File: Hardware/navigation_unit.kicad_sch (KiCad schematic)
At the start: 34 parts, among them SW1 SW_SPDT, SW2 SW_Push_Dual, U4 STM32F405RGTx, Y1 25MHz

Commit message: hardware: reorganizing components, im fucked
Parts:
- C12, C13, C25: footprint Capacitor_SMD:C_0603_1608Metric -> Capacitor_SMD:C_0402_1005Metric
- C14: footprint Capacitor_SMD:C_1206_3216Metric_Pad1.33x1.80mm_HandSolder -> Capacitor_SMD:C_0603_1608Metric
- D4, D5, D6, D7: footprint LED_SMD:LED_0805_2012Metric_Pad1.15x1.40mm_HandSolder -> LED_SMD:LED_0402_1005Metric
- FB1: footprint Inductor_SMD:L_0805_2012Metric_Pad1.05x1.20mm_HandSolder -> Inductor_SMD:L_0402_1005Metric
- R10, R11, R12, R13, R14, R15, R16, R17, R18, R9: footprint Resistor_SMD:R_0603_1608Metric_Pad0.98x0.95mm_HandSolder -> Resistor_SMD:R_0402_1005Metric
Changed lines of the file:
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@@
 			)
 		)
-		(property "Footprint" "Resistor_SMD:R_0603_1608Metric_Pad0.98x0.95mm_HandSolder"
+		(property "Footprint" "Resistor_SMD:R_0402_1005Metric"
 			(at 228.092 139.7 90)
 			(effects
@@
 			)
 		)
-		(property "Footprint" "LED_SMD:LED_0805_2012Metric_Pad1.15x1.40mm_HandSolder"
+		(property "Footprint" "LED_SMD:LED_0402_1005Metric"
 			(at 166.37 138.43 0)
 			(effects
@@
 			)
 		)
-		(property "Footprint" "Capacitor_SMD:C_1206_3216Metric_Pad1.33x1.80mm_HandSolder"
+		(property "Footprint" "Capacitor_SMD:C_0603_1608Metric"
 			(at 141.9352 36.83 0)
 			(effects
@@
 			)
 		)
-		(property "Footprint" "Resistor_SMD:R_0603_1608Metric_Pad0.98x0.95mm_HandSolder"
+		(property "Footprint" "Resistor_SMD:R_0402_1005Metric"
 			(at 235.712 139.7 90)
 			(effects
@@
 			)
 		)
-		(property "Footprint" "Capacitor_SMD:C_0603_1608Metric"
+		(property "Footprint" "Capacitor_SMD:C_0402_1005Metric"
 			(at 40.3352 144.78 0)
 			(effects
@@
 			)
 		)
-		(property "Footprint" "LED_SMD:LED_0805_2012Metric_Pad1.15x1.40mm_HandSolder"
+		(property "Footprint" "LED_SMD:LED_0402_1005Metric"
 			(at 184.15 138.43 0)
 			(effects
@@
 			)
 		)
-		(property "Footprint" "Resistor_SMD:R_0603_1608Metric_Pad0.98x0.95mm_HandSolder"
+		(property "Footprint" "Resistor_SMD:R_0402_1005Metric"
 			(at 250.952 139.7 90)
 			(effects
@@
 			)
 		)
-		(property "Footprint" "Resistor_SMD:R_0603_1608Metric_Pad0.98x0.95mm_HandSolder"
+		(property "Footprint" "Resistor_SMD:R_0402_1005Metric"
 			(at 173.99 67.818 90)
 			(effects
@@
 			)
 		)
-		(property "Footprint" "Resistor_SMD:R_0603_1608Metric_Pad0.98x0.95mm_HandSolder"
+		(property "Footprint" "Resistor_SMD:R_0402_1005Metric"
 			(at 243.332 139.7 90)
 			(effects
@@
 			)
 		)
-		(property "Footprint" "Resistor_SMD:R_0603_1608Metric_Pad0.98x0.95mm_HandSolder"
+		(property "Footprint" "Resistor_SMD:R_0402_1005Metric"
 			(at 164.592 146.05 90)
 			(effects
@@
 			)
 		)
-		(property "Footprint" "LED_SMD:LED_0805_2012Metric_Pad1.15x1.40mm_HandSolder"
+		(property "Footprint" "LED_SMD:LED_0402_1005Metric"
 			(at 175.26 138.43 0)
 			(effects
@@
 			)
 		)
-		(property "Footprint" "Capacitor_SMD:C_0603_1608Metric"
+		(property "Footprint" "Capacitor_SMD:C_0402_1005Metric"
 			(at 30.1752 144.78 0)
 			(effects
@@
 			)
 		)
-		(property "Footprint" "Inductor_SMD:L_0805_2012Metric_Pad1.05x1.20mm_HandSolder"
+		(property "Footprint" "Inductor_SMD:L_0402_1005Metric"
 			(at 232.41 56.388 90)
 			(effects
@@
 			)
 		)
-		(property "Footprint" "Capacitor_SMD:C_0603_1608Metric"
+		(property "Footprint" "Capacitor_SMD:C_0402_1005Metric"
 			(at 249.8852 101.6 0)
 			(effects
@@
 			)
 		)
-		(property "Footprint" "Resistor_SMD:R_0603_1608Metric_Pad0.98x0.95mm_HandSolder"
+		(property "Footprint" "Resistor_SMD:R_0402_1005Metric"
 			(at 182.372 146.05 90)
 			(effects
@@
 			)
 		)
-		(property "Footprint" "LED_SMD:LED_0805_2012Metric_Pad1.15x1.40mm_HandSolder"
+		(property "Footprint" "LED_SMD:LED_0402_1005Metric"
 			(at 193.04 138.43 0)
 			(effects
@@
 			)
 		)
-		(property "Footprint" "Resistor_SMD:R_0603_1608Metric_Pad0.98x0.95mm_HandSolder"
+		(property "Footprint" "Resistor_SMD:R_0402_1005Metric"
 			(at 173.482 146.05 90)
 			(effects
@@
 			)
 		)
-		(property "Footprint" "Resistor_SMD:R_0603_1608Metric_Pad0.98x0.95mm_HandSolder"
+		(property "Footprint" "Resistor_SMD:R_0402_1005Metric"
 			(at 191.262 146.05 90)
 			(effects
@@
 			)
 		)
-		(property "Footprint" "Resistor_SMD:R_0603_1608Metric_Pad0.98x0.95mm_HandSolder"
+		(property "Footprint" "Resistor_SMD:R_0402_1005Metric"
 			(at 175.26 107.188 90)
 			(effects

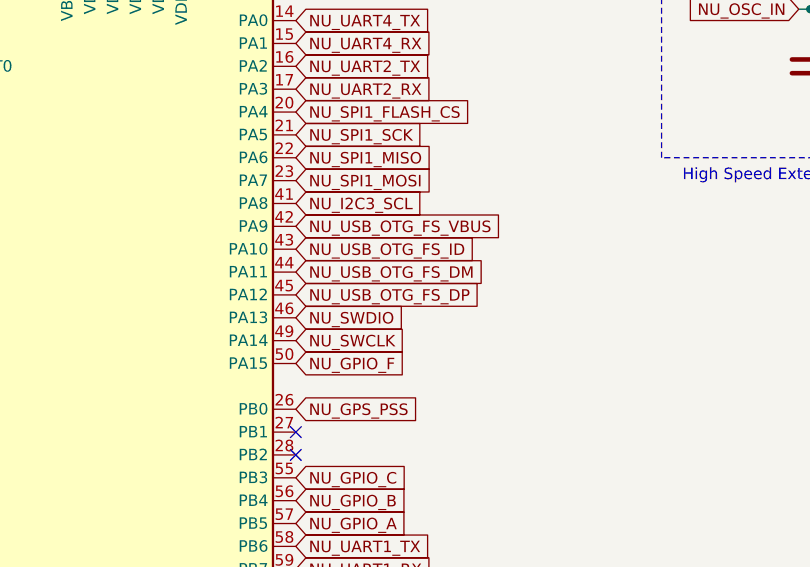
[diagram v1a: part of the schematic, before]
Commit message: usb traces, i2c, spi, sdio, and more
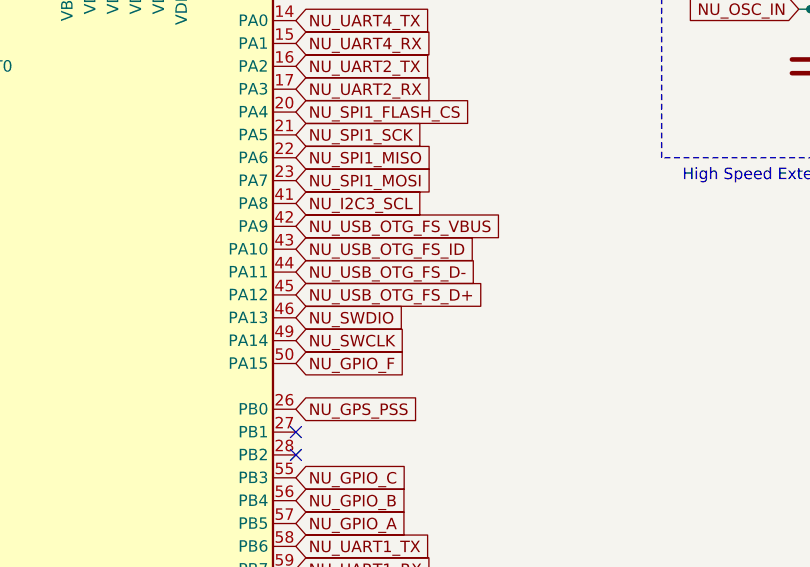
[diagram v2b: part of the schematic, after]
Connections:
- net NU_USB_OTG_FS_DM renamed NU_USB_OTG_FS_D-
- net NU_USB_OTG_FS_DP renamed NU_USB_OTG_FS_D+
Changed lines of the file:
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@@
 		)
 	)
-	(global_label "NU_USB_OTG_FS_DM"
+	(global_label "NU_USB_OTG_FS_D-"
 		(shape input)
 		(at 90.17 95.25 0)
@@
 		)
 		(property "Intersheetrefs" "${INTERSHEET_REFS}"
-			(at 112.0842 95.25 0)
+			(at 112.2052 95.25 0)
 			(effects
 				(font
@@
 		)
 	)
-	(global_label "NU_USB_OTG_FS_DP"
+	(global_label "NU_USB_OTG_FS_D+"
 		(shape input)
 		(at 90.17 97.79 0)
@@
 		)
 		(property "Intersheetrefs" "${INTERSHEET_REFS}"
-			(at 111.9028 97.79 0)
-			(effects
-				(font
+			(at 112.2052 97.79 0)
+			(effects
+				(font

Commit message: i2c sensors traces
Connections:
- net NU_SPI2_CS_IMU: no longer names the net of U4.33 (PB12)
- net NU_SPI2_MISO: no longer names the net of U4.10 (PC2)
- net NU_SPI2_MOSI: no longer names the net of U4.11 (PC3)
- net NU_SPI2_SCK: no longer names the net of U4.34 (PB13)
- no-connect marks 4 -> 8
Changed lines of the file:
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@@
+	)
+	(no_connect
+		(at 90.17 143.51)
 	)
 	(no_connect
@@
 	)
 	(no_connect
+		(at 49.53 95.25)
+	)
+	(no_connect
 		(at 49.53 110.49)
 	)
+	(no_connect
+		(at 90.17 140.97)
+	)
+	(no_connect
+		(at 49.53 97.79)
+	)
 	(wire
 		(pts
@@
 		)
 	)
-	(global_label "NU_SPI2_CS_IMU"
-		(shape input)
-		(at 90.17 140.97 0)
-		(fields_autoplaced yes)
-		(effects
-			(font
-				(size 1.27 1.27)
-			)
-			(justify left)
-		)
-		(property "Intersheetrefs" "${INTERSHEET_REFS}"
-			(at 108.879 140.97 0)
-			(effects
-				(font
-					(size 1.27 1.27)
-				)
-				(justify left)
-				(hide yes)
-			)
-		)
-	)
 	(global_label "NU_USB_OTG_FS_D-"
 		(shape input)
@@
 		)
 	)
-	(global_label "NU_SPI2_SCK"
-		(shape input)
-		(at 90.17 143.51 0)
-		(fields_autoplaced yes)
-		(effects
-			(font
-				(size 1.27 1.27)
-			)
-			(justify left)
-		)
-		(property "Intersheetrefs" "${INTERSHEET_REFS}"
-			(at 105.7947 143.51 0)
-			(effects
-				(font
-					(size 1.27 1.27)
-				)
-				(justify left)
-				(hide yes)
-			)
-		)
-	)
 	(global_label "NU_I2C2_SDA"
 		(shape input)
@@
 		)
 	)
-	(global_label "NU_SPI2_MISO"
-		(shape input)
-		(at 49.53 95.25 180)
-		(fields_autoplaced yes)
-		(effects
-			(font
-				(size 1.27 1.27)
-			)
-			(justify right)
-		)
-		(property "Intersheetrefs" "${INTERSHEET_REFS}"
-			(at 33.0586 95.25 0)
-			(effects
-				(font
-					(size 1.27 1.27)
-				)
-				(justify right)
-				(hide yes)
-			)
-		)
-	)
 	(global_label "NU_SPI1_MISO"
 		(shape input)
@@
 				(hide yes)
 			)
-		)
-	)
-	(global_label "NU_SPI2_MOSI"
-		(shape input)
-		(at 49.53 97.79 180)
-		(fields_autoplaced yes)
-		(effects
-			(font
-				(size 1.27 1.27)
-			)
-			(justify right)
-		)
-		(property "Intersheetrefs" "${INTERSHEET_REFS}"
-			(at 33.0586 97.79 0)
-			(effects
-				(font
-					(size 1.27 1.27)
-				)
-				(justify right)
-				(hide yes)
-			)
